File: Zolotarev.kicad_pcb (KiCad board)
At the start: 2 copper layers, 185 x 185 mm, 172 parts, among them J1 RF_IN, J2 RF_OUT, J3 Conn_02x05_Odd_Even, K1 G5LE-1, K10 G5LE-1, K11 G5LE-1, K12 G5LE-1, K13 G5LE-1, K14 G5LE-1, K2 G5LE-1, K3 G5LE-1, K4 G5LE-1, K5 G5LE-1, K6 G5LE-1, K7 G5LE-1, K8 G5LE-1, K9 G5LE-1

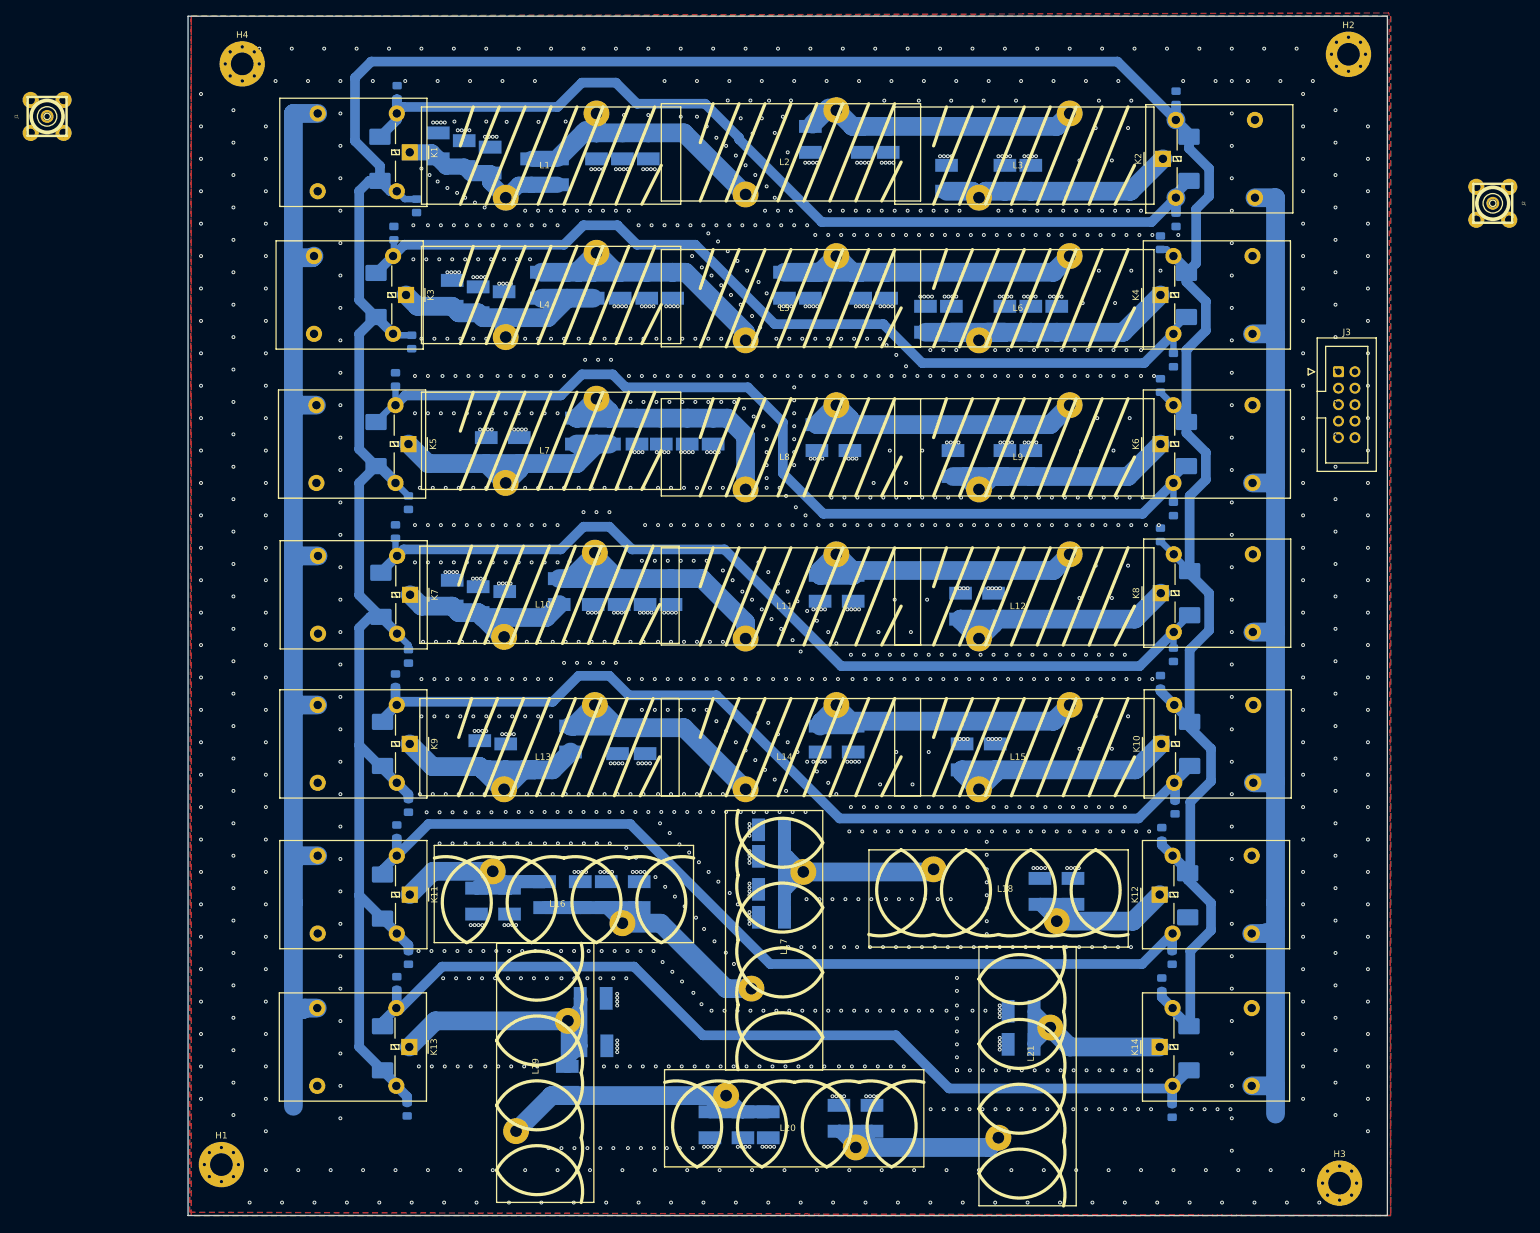
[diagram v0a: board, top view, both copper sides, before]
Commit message: silkmask partly added
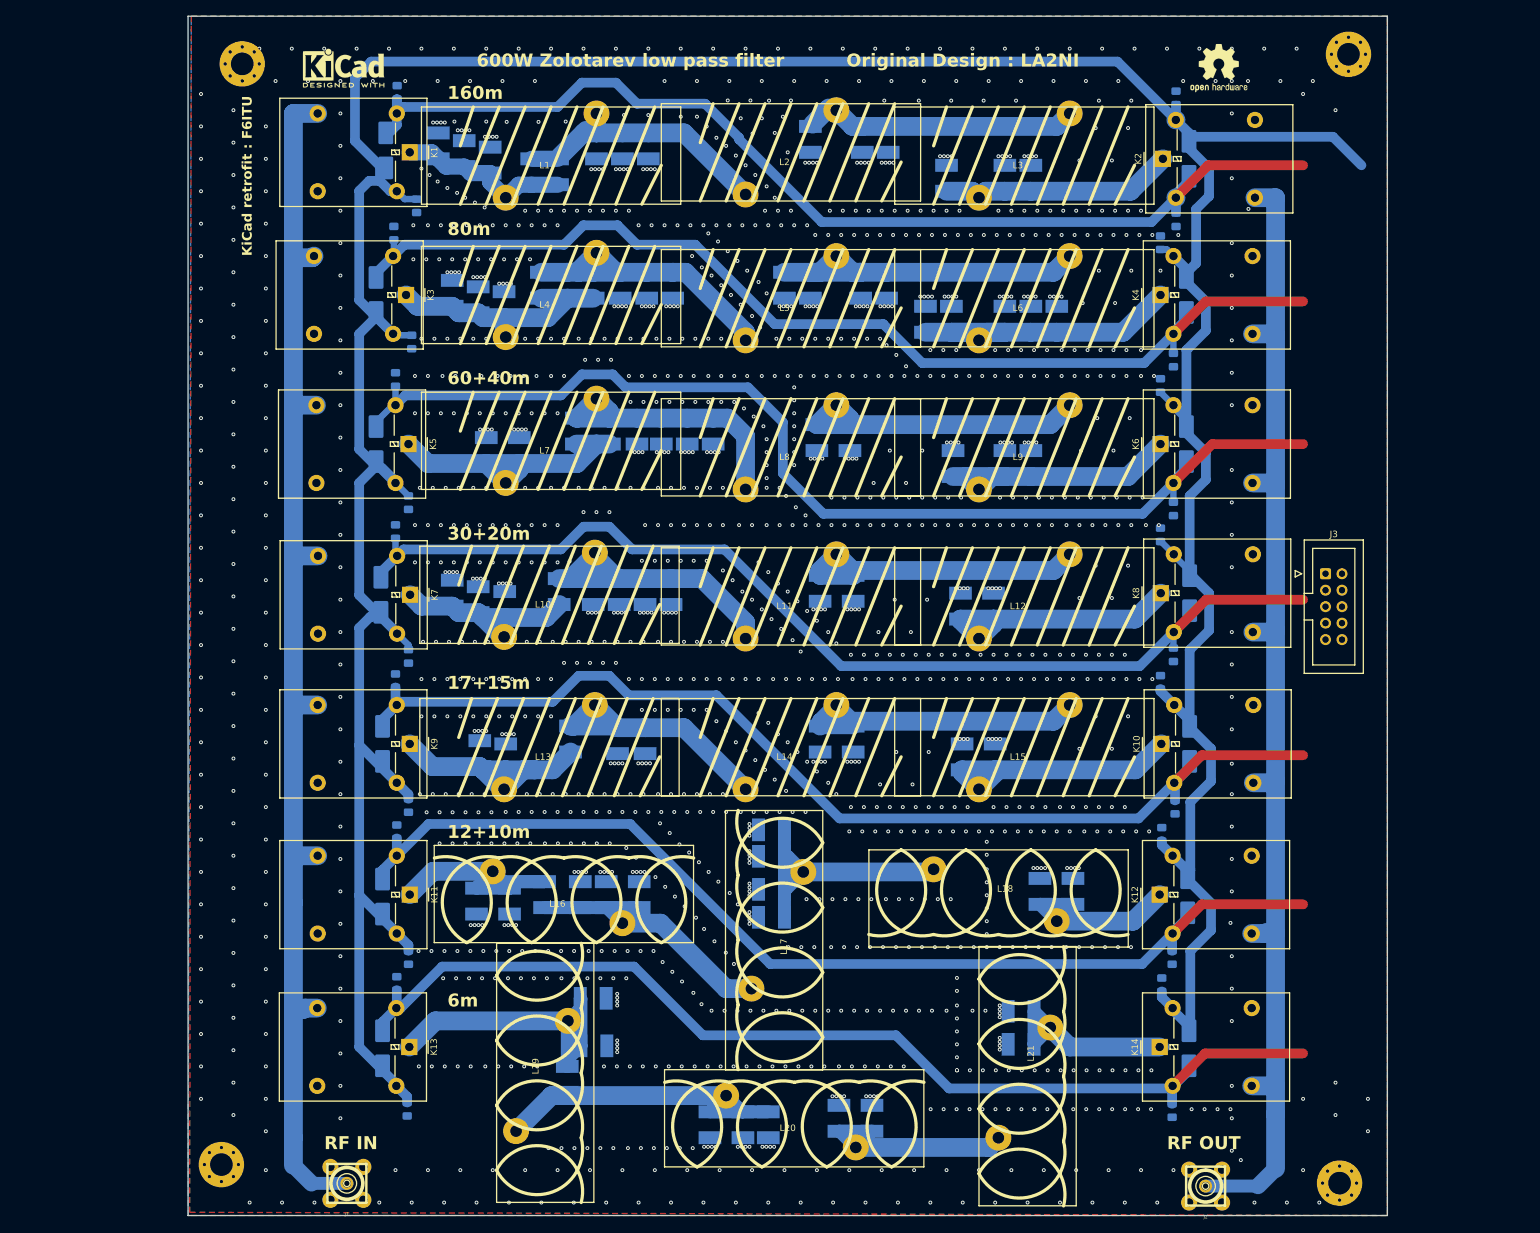
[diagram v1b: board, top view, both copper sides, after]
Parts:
- added REF**: KiCad-Logo2_5mm_SilkScreen, Symbol:KiCad-Logo2_5mm_SilkScreen, F.Cu at (69.0, 28.0)
- added REF**: OSHW-Logo2_9.8x8mm_SilkScreen, Symbol:OSHW-Logo2_9.8x8mm_SilkScreen, F.Cu at (204.0, 28.0)
- D1, D10, D11, D12, D13, D14, D2, D3, D4, D5, D6, D7, D8, D9: footprint Diode_SMD:D_SMC -> Diode_SMD:D_SMB_Handsoldering
- moved J1 171.0 mm to (69.5, 200.0), turned to 0 degrees
- moved J2 157.9 mm to (202.0, 200.5), turned to 0 degrees
- moved J3 31.2 mm to (220.5, 106.0)
- moved D1 1.58 mm to (75.5, 40.7)
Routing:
- net +12V: track 556.4 -> 584.8 mm
- net 12+10m: track 141.8 -> 167.2 mm
- net 60+40m: track 150.8 -> 173.3 mm
- net 6m: track 143.1 -> 165.3 mm
- net 80m: track 145.7 -> 167.8 mm
- net 30+20m: track 145.3 -> 167.3 mm
- net 17+15m: track 145.8 -> 167.5 mm
- net 160m: track 145.8 -> 166.3 mm
- net RF_OUT: track 166.4 -> 186.7 mm
- net RF_IN: track 179.1 -> 197.7 mm
- net GND: vias 1632 -> 1534
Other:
- board text added: "12+10m"
- board text added: "160m"
- board text added: "17+15m"
- board text added: "30+20m"
- board text added: "60+40m"
- board text added: "600W Zolotarev low pass filter Original Design : LA2NI"
- board text added: "6m"
- board text added: "80m"
- board text added: "KiCad retrofit : F6ITU"
- board text added: "RF IN"
- board text added: "RF OUT"

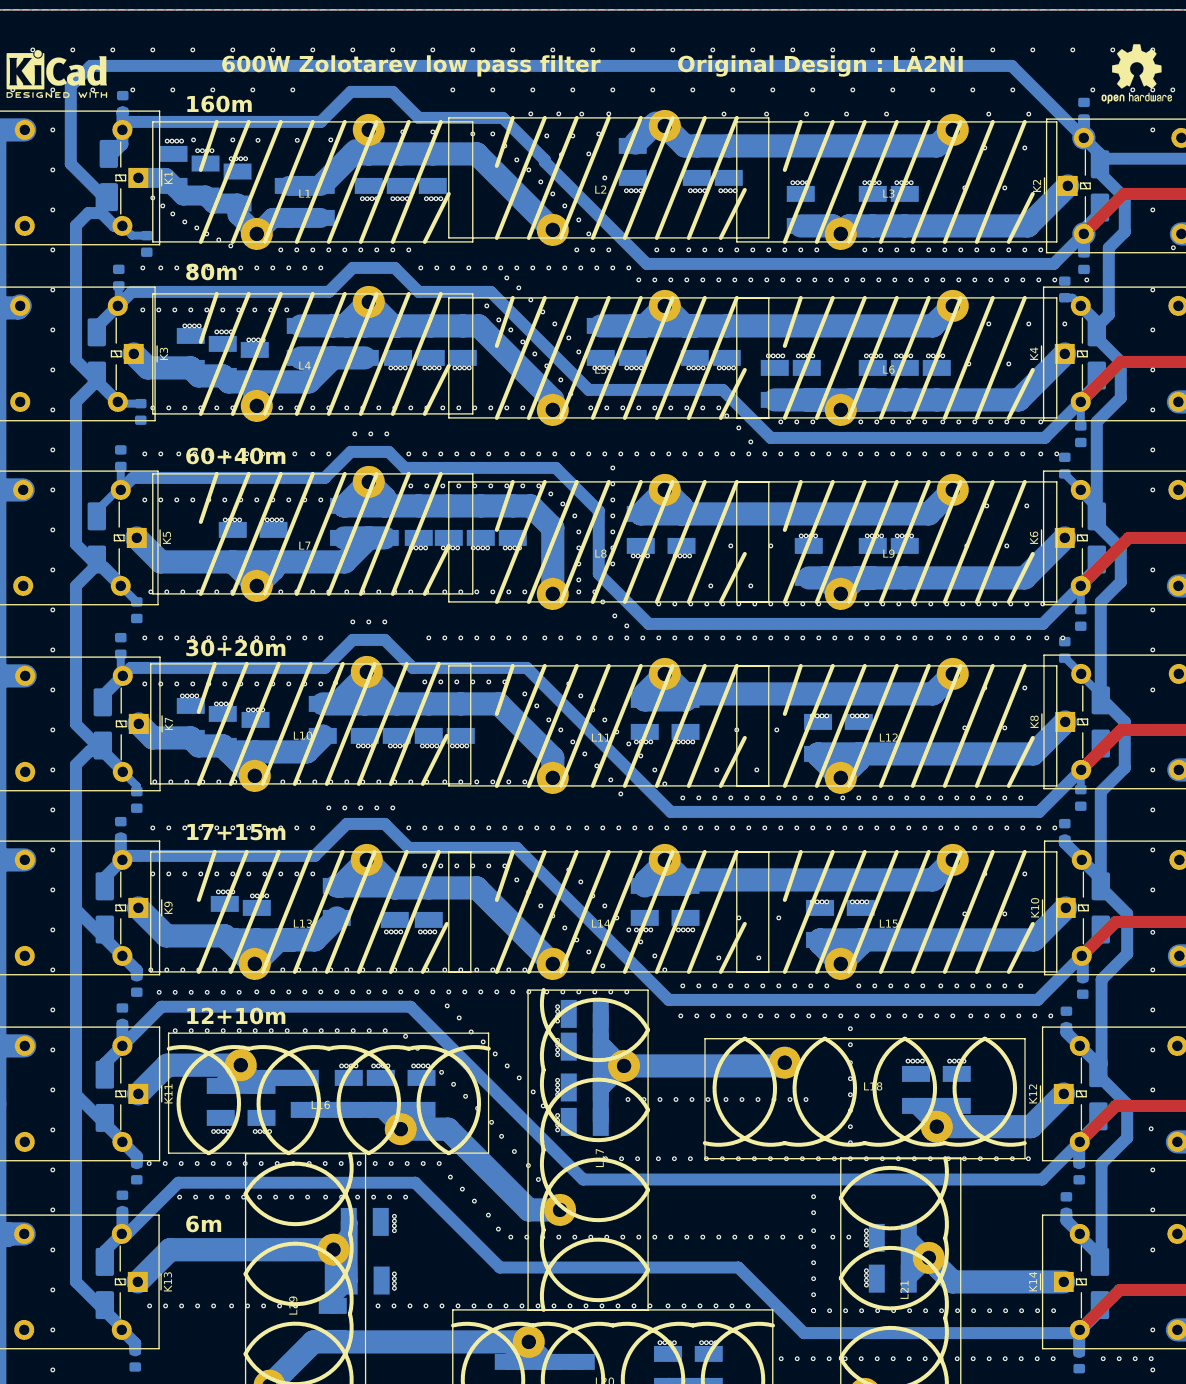
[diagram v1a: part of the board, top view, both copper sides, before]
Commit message: diodes changed for smb, silk cleaned
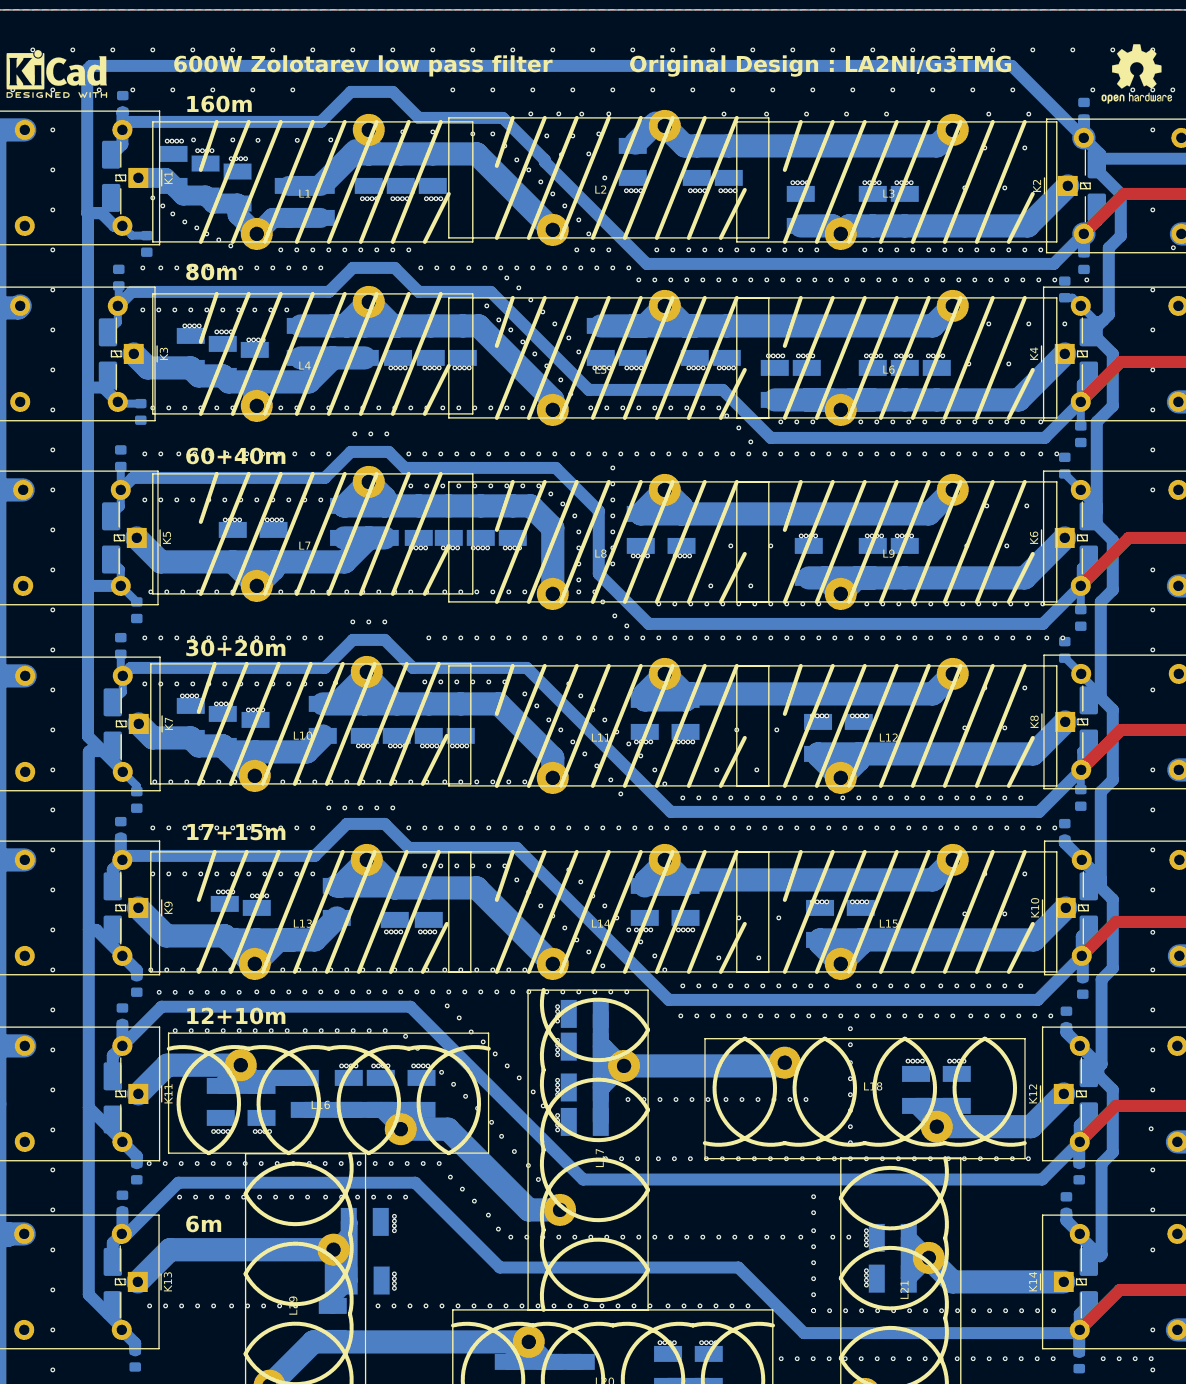
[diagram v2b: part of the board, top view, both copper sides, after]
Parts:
- moved D3 1.80 mm to (75.8, 86.0)
- moved D10 1.50 mm to (198.0, 132.2)
- moved D11 1.50 mm to (198.0, 109.0)
- moved D2 1.40 mm to (75.4, 63.0)
- moved D8 1.40 mm to (198.0, 179.2)
- moved D4 1.25 mm to (76.0, 109.2)
- moved D6 1.20 mm to (198.0, 155.6)
- moved D9 1.02 mm to (76.0, 156.0)
- moved D12 1.00 mm to (198.0, 86.0)
- moved D13 1.00 mm to (198.0, 63.0)
- moved D5 1.00 mm to (76.0, 132.2)
- moved D7 1.00 mm to (76.0, 179.2)
- moved D14 0.40 mm to (199.0, 42.0)
- moved D1 0.32 mm to (75.8, 40.8)
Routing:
- net +12V: track 584.8 -> 567.9 mm
- net 160m: track 166.3 -> 167.4 mm
- net 12+10m: track 167.2 -> 167.9 mm
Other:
- board text added: "600W Zolotarev low pass filter Original Design : LA2NI/G3TMG"
- board text removed: "600W Zolotarev low pass filter Original Design : LA2NI"
